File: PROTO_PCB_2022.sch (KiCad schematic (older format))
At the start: 20 parts, among them J1 HORN_EN1, J10 ECU_KILL_2, J11 ECU_KILL_3, J12 12V_EXTRA, J2 BRAKELIGHTS_EN1, J3 BRAKELIGHTS_CONN, J4 STARTER_MOTOR_EN, J5 VESC_EN_SIGNAL, J6 HORN_CONN, J7 12V_BATT1, J8 ECU_POWER_DIST, J9 ECU_KILL_1, Q1 HORN_MOSFET1, Q2 BRAKELIGHTS_MOSFET1, U1 LD1117S50TR_SOT223

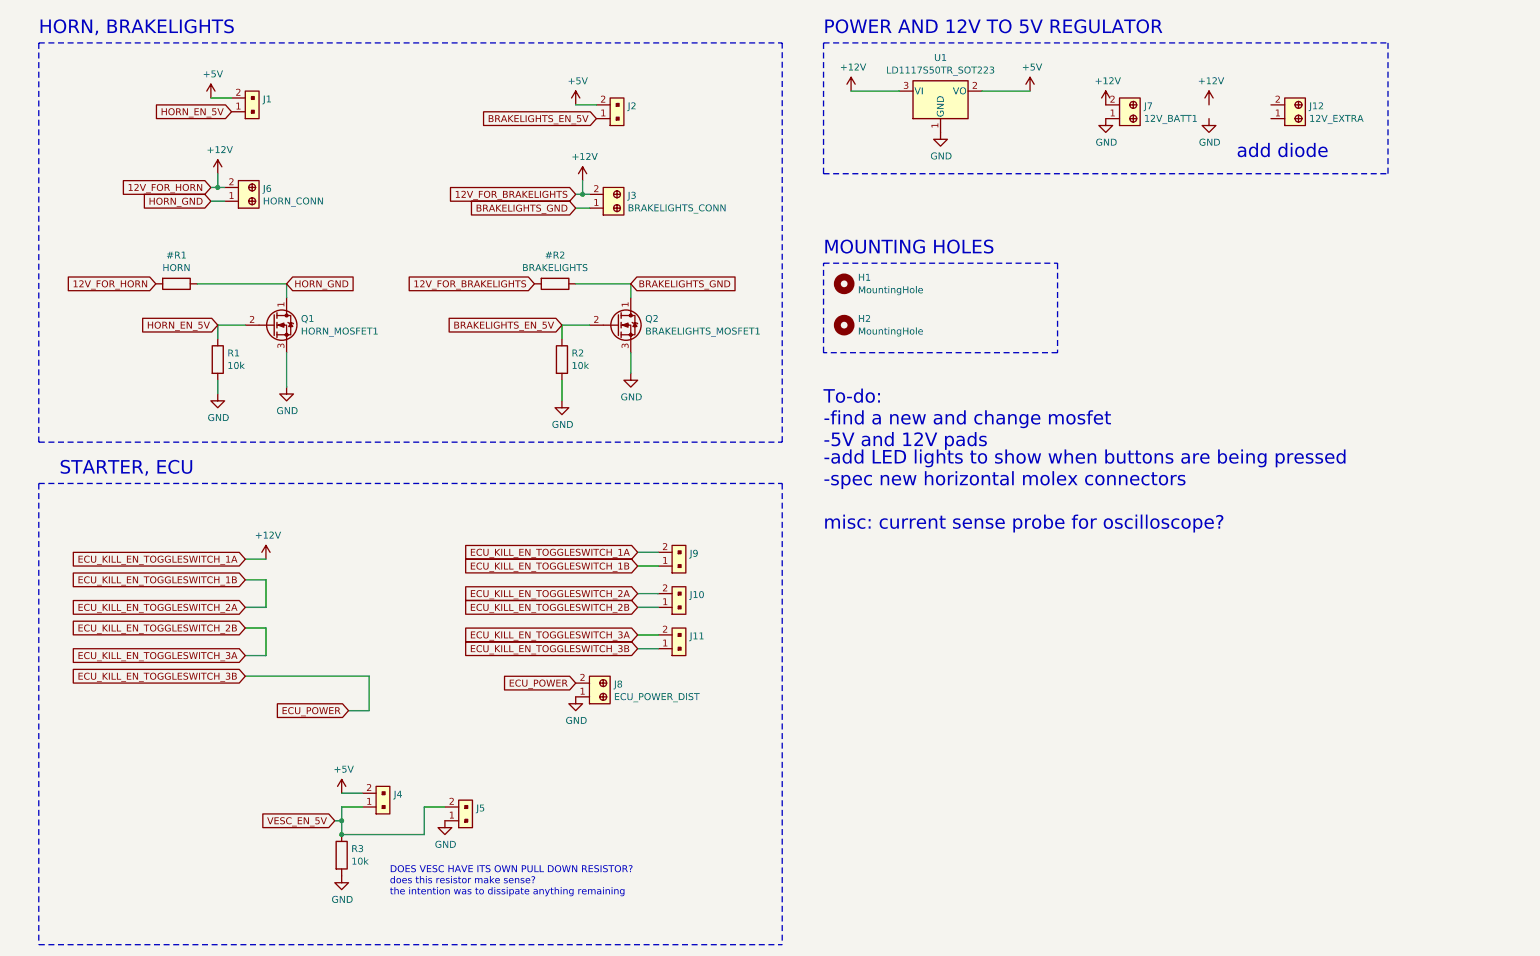
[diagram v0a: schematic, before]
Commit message: changed mosfet
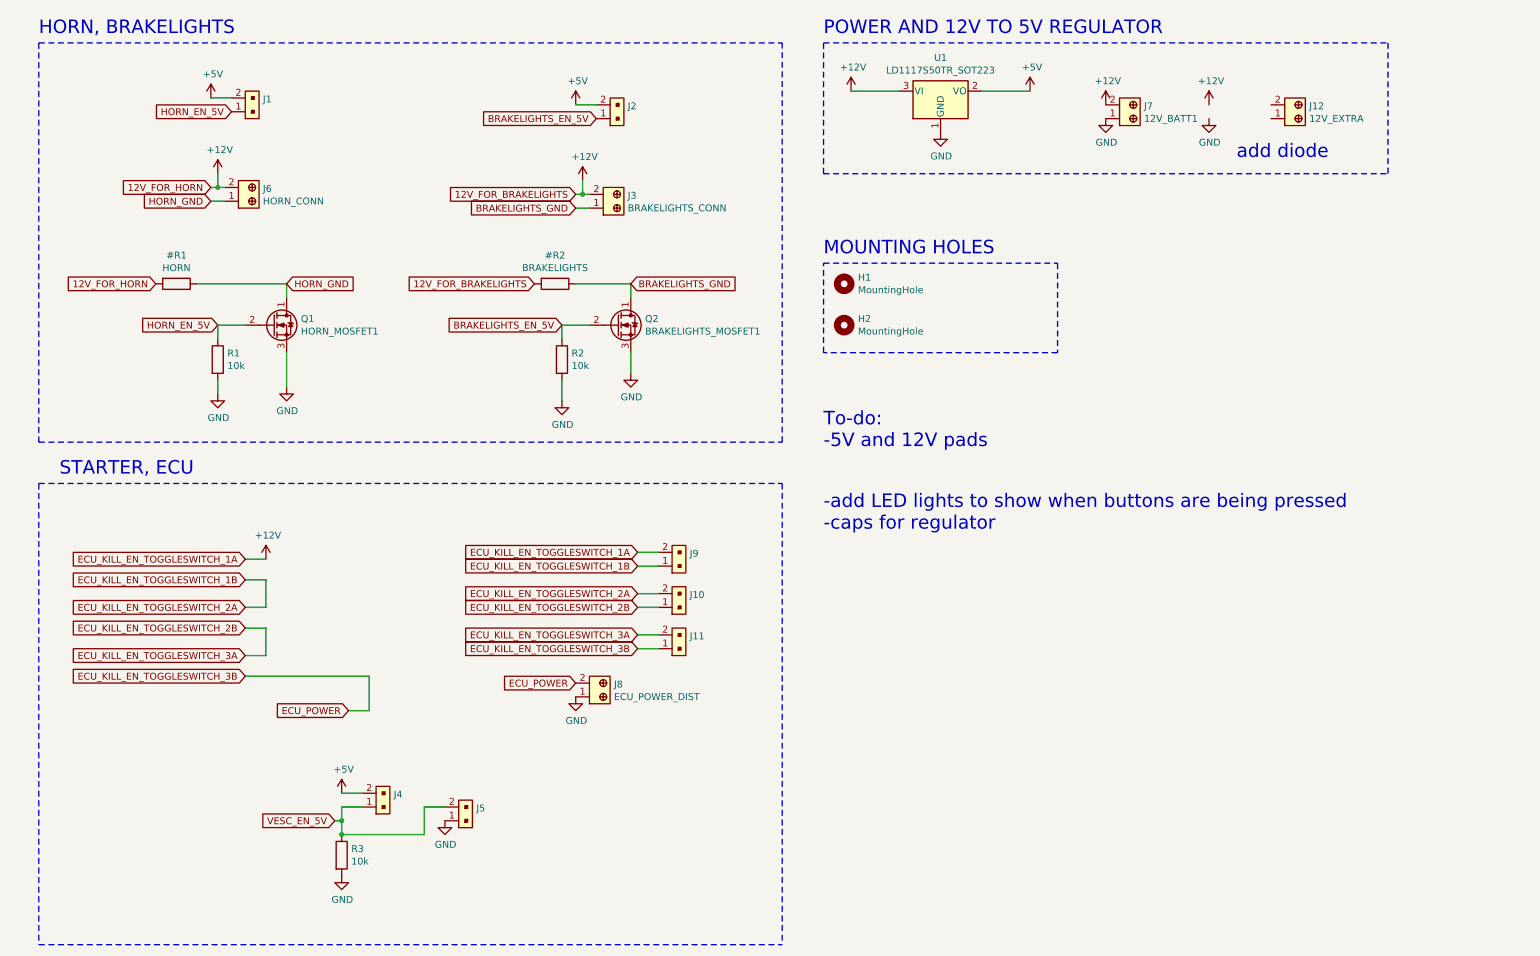
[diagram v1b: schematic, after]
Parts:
- Q1, Q2: DigiKeyPN RK7002BMT116CT-ND -> ZXMN3F30FHCT-ND; MPN RK7002BMT116 -> ZXMN3F30FHTA
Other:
- note added: "-add LED lights to show when buttons are being pressed\n-caps for regulator\n -spec new horizontal molex connectors\nmisc: current sense probe for oscilloscope?"
- note added: "To-do:\n-5V and 12V pads\n"
- note removed: "-add LED lights to show when buttons are being pressed\n-spec new horizontal molex connectors\n\nmisc: current sense probe for oscilloscope?"
- note removed: "DOES VESC HAVE ITS OWN PULL DOWN RESISTOR?\ndoes this resistor make sense?\nthe intention was to dissipate anything remaining"
- note removed: "To-do:\n-find a new and change mosfet\n-5V and 12V pads\n"
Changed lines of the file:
@@
 	6500 2500 8200 2500
-Wire Notes Line
-	8200 2500 8200 3150
 Wire Notes Line
 	8200 3150 6500 3150
@@
 	1    0    0    -1
 $EndComp
-Text Notes 3350 7100 0    50   ~ 0
-DOES VESC HAVE ITS OWN PULL DOWN RESISTOR?\ndoes this resistor make sense?\nthe intention was to dissipate anything remaining
 Connection ~ 3000 6650
 $Comp
@@
 F 1 "HORN_MOSFET1" H 2704 2905 50  0000 L CNN
 F 2 "Package_TO_SOT_SMD:SOT-23" H 2700 3050 50  0001 C CNN
-F 3 "https://www.digikey.ca/en/products/detail/rohm-semiconductor/RK7002BMT116/4924083" H 2500 2950 50  0001 C CNN
-F 4 "RK7002BMT116" H 2500 2950 50  0001 C CNN "MPN"
-F 5 "RK7002BMT116CT-ND" H 2500 2950 50  0001 C CNN "DigiKeyPN"
+F 3 "https://www.digikey.ca/en/products/detail/diodes-incorporated/ZXMN3F30FHTA/1827752" H 2500 2950 50  0001 C CNN
+F 4 "ZXMN3F30FHTA" H 2500 2950 50  0001 C CNN "MPN"
+F 5 "ZXMN3F30FHCT-ND" H 2500 2950 50  0001 C CNN "DigiKeyPN"
 	1    2500 2950
 	1    0    0    -1
@@
 	2600 2750 2600 2650
 Text Notes 6500 3850 0    98   ~ 0
-To-do:\n-find a new and change mosfet\n-5V and 12V pads\n
+To-do:\n-5V and 12V pads\n
 Text Notes 9500 1750 0    98   ~ 0
 add diode
@@
 Wire Notes Line
 	6500 1850 10600 1850
+Wire Wire Line
+	2600 3150 2600 3400
+Text Notes 6500 4450 0    98   ~ 0
+-add LED lights to show when buttons are being pressed\n-caps for regulator\n -spec new horizontal molex connectors\nmisc: current sense probe for oscilloscope?
 $Comp
 L Device:Q_NMOS_DGS Q2
-U 1 1 618C50B5
+U 1 1 62652563
 P 5000 2950
-F 0 "Q2" H 5205 2996 50  0000 L CNN
-F 1 "BRAKELIGHTS_MOSFET1" H 5205 2905 50  0000 L CNN
+F 0 "Q2" H 5204 2996 50  0000 L CNN
+F 1 "BRAKELIGHTS_MOSFET1" H 5204 2905 50  0000 L CNN
 F 2 "Package_TO_SOT_SMD:SOT-23" H 5200 3050 50  0001 C CNN
-F 3 "https://www.digikey.ca/en/products/detail/rohm-semiconductor/RK7002BMT116/4924083" H 5000 2950 50  0001 C CNN
-F 4 "RK7002BMT116" H 5000 2950 50  0001 C CNN "MPN"
-F 5 "RK7002BMT116CT-ND" H 5000 2950 50  0001 C CNN "DigiKeyPN"
+F 3 "https://www.digikey.ca/en/products/detail/diodes-incorporated/ZXMN3F30FHTA/1827752" H 5000 2950 50  0001 C CNN
+F 4 "ZXMN3F30FHTA" H 5000 2950 50  0001 C CNN "MPN"
+F 5 "ZXMN3F30FHCT-ND" H 5000 2950 50  0001 C CNN "DigiKeyPN"
 	1    5000 2950
 	1    0    0    -1
 $EndComp
-Wire Wire Line
-	2600 3150 2600 3400
-Text Notes 6500 4450 0    98   ~ 0
--add LED lights to show when buttons are being pressed\n-spec new horizontal molex connectors\n\nmisc: current sense probe for oscilloscope?
+Wire Notes Line
+	8200 2500 8200 3150
 $EndSCHEMATC

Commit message: almost final version
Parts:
- removed J10: ECU_KILL_2, Footprint Library:Molex_Proto_Microfit_Footprint, symbol PROTO_PCB_2022-rescue:B2B-PH-K-S_LF__SN_-dk_Rectangular-Connectors-Headers-Male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
- removed J11: ECU_KILL_3, Footprint Library:Molex_Proto_Microfit_Footprint, symbol PROTO_PCB_2022-rescue:B2B-PH-K-S_LF__SN_-dk_Rectangular-Connectors-Headers-Male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
- removed J9: ECU_KILL_1, Footprint Library:Molex_Proto_Microfit_Footprint, symbol PROTO_PCB_2022-rescue:B2B-PH-K-S_LF__SN_-dk_Rectangular-Connectors-Headers-Male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
- added C1: 1u, Capacitor_SMD:C_1206_3216Metric, symbol Device:C
- added C2: 4.7u, Capacitor_SMD:C_1206_3216Metric, symbol Device:C
- added D1, D2: LED, Resistor_SMD:R_0603_1608Metric, symbol Device:LED
- added F1: Fuse, Fuse:Fuseholder_Blade_ATO_Littelfuse_Pudenz_2_Pin, symbol Device:Fuse
- added J10: ECU_3, TerminalBlock_Phoenix:TerminalBlock_Phoenix_PT-1,5-2-5.0-H_1x02_P5.00mm_Horizontal, symbol PROTO_PCB_2022-rescue:1935161-dk_Terminal-Blocks-Wire-to-Board
- added J8: ECU_1, TerminalBlock_Phoenix:TerminalBlock_Phoenix_PT-1,5-2-5.0-H_1x02_P5.00mm_Horizontal, symbol PROTO_PCB_2022-rescue:1935161-dk_Terminal-Blocks-Wire-to-Board
- added J9: ECU_2, TerminalBlock_Phoenix:TerminalBlock_Phoenix_PT-1,5-2-5.0-H_1x02_P5.00mm_Horizontal, symbol PROTO_PCB_2022-rescue:1935161-dk_Terminal-Blocks-Wire-to-Board
- added R1, R4: 4.7k, Resistor_SMD:R_1206_3216Metric, symbol Device:R
- added TP1, TP2, TP3: TestPoint, TestPoint:TestPoint_Keystone_5015_Micro-Minature, symbol Connector:TestPoint
- J1: footprint Footprint Library:Molex_Proto_Microfit_Footprint -> footprints:436500201; DigiKeyPN WM10657-ND -> (none); MPN 0430450227 -> 0436500201
- J11: renamed from J7; value 12V_BATT1 -> 12V_IN
- J12: value 12V_EXTRA -> 12V_OUT_EXTRA
- J3: renamed from J4; footprint Footprint Library:Molex_Proto_Microfit_Footprint -> footprints:436500201; DigiKeyPN WM10657-ND -> (none); MPN 0430450227 -> 0436500201
- J4: renamed from J5; footprint Footprint Library:Molex_Proto_Microfit_Footprint -> footprints:436500201; DigiKeyPN WM10657-ND -> (none); MPN 0430450227 -> 0436500201
- J6: renamed from J2; footprint Footprint Library:Molex_Proto_Microfit_Footprint -> footprints:436500201; DigiKeyPN WM10657-ND -> (none); MPN 0430450227 -> 0436500201
- R2: renamed from R1; footprint Resistor_SMD:R_0805_2012Metric -> Resistor_SMD:R_1206_3216Metric; DigikeyPN 311-10.0CRCT-ND -> (none); MPN RC0805FR-0710RL -> (none)
- R3: footprint Resistor_SMD:R_0603_1608Metric -> Resistor_SMD:R_1206_3216Metric
- R5: renamed from R2; footprint Resistor_SMD:R_0805_2012Metric -> Resistor_SMD:R_1206_3216Metric; DigikeyPN 311-10.0CRCT-ND -> (none); MPN RC0805FR-0710RL -> (none)
- renumbered J6 to J2, J8 to J5, J3 to J7
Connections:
- net +12V: now also J12.2, C1.1, F1.2, J8.2, TP1.1; no longer J11.2
- net +5V: now also C2.1, TP2.1
- net BRAKELIGHTS_EN_5V: now also D2.2 (A)
- net ECU_KILL_EN_TOGGLESWITCH_1B: now also J8.1, J9.2
- net ECU_KILL_EN_TOGGLESWITCH_2B: now also J10.2, J9.1
- net ECU_KILL_EN_TOGGLESWITCH_3B: now also J10.1
- net GND: now also J12.1, C1.2, C2.2, R1.2, R4.2, TP3.1
- net HORN_EN_5V: now also D1.2 (A)
- new net: D1.1 (K), R1.1
- new net: D2.1 (K), R4.1
- new net BATT_12V: F1.1, J11.2
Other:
- note removed: "-add LED lights to show when buttons are being pressed\n-caps for regulator\n -spec new horizontal molex connectors\nmisc: current sense probe for oscilloscope?"
- note removed: "To-do:\n-5V and 12V pads\n"
- note removed: "add diode"
- moved on the sheet: H1, H2, J11, J12, R2, R5, U1

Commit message: schematic done
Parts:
- removed J1: HORN_EN1, footprints:436500201, symbol PROTO_PCB_2022-rescue:B2B-PH-K-S_LF__SN_-dk_Rectangular-Connectors-Headers-Male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
- removed J10: ECU_3, TerminalBlock_Phoenix:TerminalBlock_Phoenix_PT-1,5-2-5.0-H_1x02_P5.00mm_Horizontal, symbol PROTO_PCB_2022-rescue:1935161-dk_Terminal-Blocks-Wire-to-Board
- removed J12: 12V_OUT_EXTRA, TerminalBlock_Phoenix:TerminalBlock_Phoenix_PT-1,5-2-5.0-H_1x02_P5.00mm_Horizontal, symbol PROTO_PCB_2022-rescue:1935161-dk_Terminal-Blocks-Wire-to-Board
- removed J2: HORN_CONN, TerminalBlock_Phoenix:TerminalBlock_Phoenix_PT-1,5-2-5.0-H_1x02_P5.00mm_Horizontal, symbol PROTO_PCB_2022-rescue:1935161-dk_Terminal-Blocks-Wire-to-Board
- removed J5: ECU_POWER_DIST, TerminalBlock_Phoenix:TerminalBlock_Phoenix_PT-1,5-2-5.0-H_1x02_P5.00mm_Horizontal, symbol PROTO_PCB_2022-rescue:1935161-dk_Terminal-Blocks-Wire-to-Board
- removed J7: BRAKELIGHTS_CONN, TerminalBlock_Phoenix:TerminalBlock_Phoenix_PT-1,5-2-5.0-H_1x02_P5.00mm_Horizontal, symbol PROTO_PCB_2022-rescue:1935161-dk_Terminal-Blocks-Wire-to-Board
- removed J8: ECU_1, TerminalBlock_Phoenix:TerminalBlock_Phoenix_PT-1,5-2-5.0-H_1x02_P5.00mm_Horizontal, symbol PROTO_PCB_2022-rescue:1935161-dk_Terminal-Blocks-Wire-to-Board
- removed J9: ECU_2, TerminalBlock_Phoenix:TerminalBlock_Phoenix_PT-1,5-2-5.0-H_1x02_P5.00mm_Horizontal, symbol PROTO_PCB_2022-rescue:1935161-dk_Terminal-Blocks-Wire-to-Board
- removed R5: 10k, Resistor_SMD:R_1206_3216Metric, symbol Device:R
- added F2: 5A, Fuse:Fuseholder_Blade_Mini_Keystone_3568, symbol Device:Fuse
- added F3, F4: 2A, Fuse:Fuseholder_Blade_Mini_Keystone_3568, symbol Device:Fuse
- added F5, F6, F7: 1A, Fuse:Fuseholder_Blade_Mini_Keystone_3568, symbol Device:Fuse
- added H3, H4: MountingHole, MountingHole:MountingHole_3.2mm_M3, symbol Mechanical:MountingHole
- added J10: 12V_OUT_AUX, Connector_Molex:Molex_Micro-Fit_3.0_43650-0200_1x02_P3.00mm_Horizontal, symbol PROTO_PCB_2022-rescue:B2B-PH-K-S_LF__SN_-dk_Rectangular-Connectors-Headers-Male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
- added J11: SW_START, Connector_Molex:Molex_Micro-Fit_3.0_43650-0200_1x02_P3.00mm_Horizontal, symbol PROTO_PCB_2022-rescue:B2B-PH-K-S_LF__SN_-dk_Rectangular-Connectors-Headers-Male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
- added J12: VESC_START, Connector_Molex:Molex_Micro-Fit_3.0_43650-0200_1x02_P3.00mm_Horizontal, symbol PROTO_PCB_2022-rescue:B2B-PH-K-S_LF__SN_-dk_Rectangular-Connectors-Headers-Male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
- added J13: 5V_OUT_AUX, Connector_Molex:Molex_Micro-Fit_3.0_43650-0200_1x02_P3.00mm_Horizontal, symbol PROTO_PCB_2022-rescue:B2B-PH-K-S_LF__SN_-dk_Rectangular-Connectors-Headers-Male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
- added J2: SW_KILL_DRIVER, Connector_Molex:Molex_Micro-Fit_3.0_43650-0200_1x02_P3.00mm_Horizontal, symbol PROTO_PCB_2022-rescue:B2B-PH-K-S_LF__SN_-dk_Rectangular-Connectors-Headers-Male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
- added J5: ECU_POWER, Connector_Molex:Molex_Micro-Fit_3.0_43650-0200_1x02_P3.00mm_Horizontal, symbol PROTO_PCB_2022-rescue:B2B-PH-K-S_LF__SN_-dk_Rectangular-Connectors-Headers-Male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
- added J7: 12V_OUT_HORN, Connector_Molex:Molex_Micro-Fit_3.0_43650-0200_1x02_P3.00mm_Horizontal, symbol PROTO_PCB_2022-rescue:B2B-PH-K-S_LF__SN_-dk_Rectangular-Connectors-Headers-Male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
- added J8: BRAKELIGHT_POWER, Connector_Molex:Molex_Micro-Fit_3.0_43650-0200_1x02_P3.00mm_Horizontal, symbol PROTO_PCB_2022-rescue:B2B-PH-K-S_LF__SN_-dk_Rectangular-Connectors-Headers-Male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
- added J9: 12V_OUT_TEL, Connector_Molex:Molex_Micro-Fit_3.0_43650-0200_1x02_P3.00mm_Horizontal, symbol PROTO_PCB_2022-rescue:B2B-PH-K-S_LF__SN_-dk_Rectangular-Connectors-Headers-Male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
- D1, D2: footprint Resistor_SMD:R_0603_1608Metric -> LED_SMD:LED_1206_3216Metric
- F1: value Fuse -> 10A; footprint Fuse:Fuseholder_Blade_ATO_Littelfuse_Pudenz_2_Pin -> Fuse:Fuseholder_Blade_Mini_Keystone_3568
- H1, H2: footprint MountingHole:MountingHole_2.7mm_M2.5 -> MountingHole:MountingHole_3.2mm_M3
- J1: renamed from J11; value 12V_IN -> 12V_BATT; footprint TerminalBlock_Phoenix:TerminalBlock_Phoenix_PT-1,5-2-5.0-H_1x02_P5.00mm_Horizontal -> Connector_Molex:Molex_Micro-Fit_3.0_43650-0200_1x02_P3.00mm_Horizontal
- J3: value STARTER_MOTOR_EN -> SW_KILL_LEFT; footprint footprints:436500201 -> Connector_Molex:Molex_Micro-Fit_3.0_43650-0200_1x02_P3.00mm_Horizontal
- J4: value VESC_EN_SIGNAL -> SW_KILL_RIGHT; footprint footprints:436500201 -> Connector_Molex:Molex_Micro-Fit_3.0_43650-0200_1x02_P3.00mm_Horizontal
- J6: value BRAKELIGHTS_EN1 -> SW_BRAKE; footprint footprints:436500201 -> Connector_Molex:Molex_Micro-Fit_3.0_43650-0200_1x02_P3.00mm_Horizontal
- Q1: value HORN_MOSFET1 -> MOSFET_ECU
- Q2: value BRAKELIGHTS_MOSFET1 -> MOSFET_BRAKE_LIGHT
- R1: value 4.7k -> 1k
- R3: value 10k -> 1k
- R4: value 4.7k -> 10k
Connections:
- net +12V: now also F1.1, F2.2, F3.2, F4.2, F5.2, F6.2; no longer F1.2
- net +5V: now also J6.1, F7.2, J2.1; no longer J3.2, J6.2
- net GND: now also J1.2, J10.1, J13.1, J7.1, J9.1; no longer J1.1, J4.1
- net at R4.1: now also D2.2 (A), J6.2, Q2.2 (G); no longer D2.1 (K)
- removed net BATT_12V: F1.1, J1.2
- removed net BRAKELIGHTS_EN_5V: D2.2 (A), J6.1, Q2.2 (G)
- net BRAKELIGHTS_GND: no longer names the net of Q2.1 (D)
- net BRAKELIGHTS_GND: now also J8.1
- net HORN_EN_5V: no longer names the net of D1.2 (A), Q1.2 (G), R2.1
- net HORN_EN_5V: now also J4.2
- net HORN_GND: no longer names the net of Q1.1 (D)
- net HORN_GND: now also J5.1
- removed net VESC_EN_5V: J3.1, J4.2, R3.1
- new net: F1.2, J1.1
- new net: F3.1, J7.2
- new net: F5.1, J9.2
- new net: F6.1, J10.2
- new net: J2.2, J3.1
- new net: J3.2, J4.1
- new net: F2.1, J5.2
- new net: F7.1, J13.2
- new net: D2.1 (K), R3.1
- new net: F4.1, J8.2
- new net: J11.2, J12.1
- new net: J11.1, J12.2
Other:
- note removed: "HORN, BRAKELIGHTS"
- note removed: "MOUNTING HOLES"
- note removed: "POWER AND 12V TO 5V REGULATOR"
- note removed: "STARTER, ECU\n"
- moved on the sheet: C1, C2, F1, H1, H2, J1, TP1, TP2, TP3, U1

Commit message: finished PCB layout
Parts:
- J1: footprint Connector_Molex:Molex_Micro-Fit_3.0_43650-0200_1x02_P3.00mm_Horizontal -> TerminalBlock_Phoenix:TerminalBlock_Phoenix_PT-1,5-2-5.0-H_1x02_P5.00mm_Horizontal
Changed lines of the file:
@@
 F 0 "J1" V 1291 1072 50  0000 R CNN
 F 1 "12V_BATT" V 1200 1072 50  0000 R CNN
-F 2 "Connector_Molex:Molex_Micro-Fit_3.0_43650-0200_1x02_P3.00mm_Horizontal" H 1400 1350 60  0001 L CNN
+F 2 "TerminalBlock_Phoenix:TerminalBlock_Phoenix_PT-1,5-2-5.0-H_1x02_P5.00mm_Horizontal" H 1400 1350 60  0001 L CNN
 F 3 "https://media.digikey.com/pdf/Data%20Sheets/Phoenix%20Contact%20PDFs/1935161.pdf" H 1400 1450 60  0001 L CNN
 F 4 "277-1667-ND" H 1400 1550 60  0001 L CNN "Digi-Key_PN"
